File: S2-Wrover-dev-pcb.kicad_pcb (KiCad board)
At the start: 2 copper layers, 99.1 x 50 mm, 29 parts, among them J1 USB_C_Receptacle_USB2.0, J2 Jack-DC, P1 CONN_02X13, P3 CONN_02X13, SW1 RESET, SW2 BOOT, U1 MCP1700-1202E_SOT23, U2 ESP32-S2-WROVER, U3 TPS2113APW, U4 TP4056

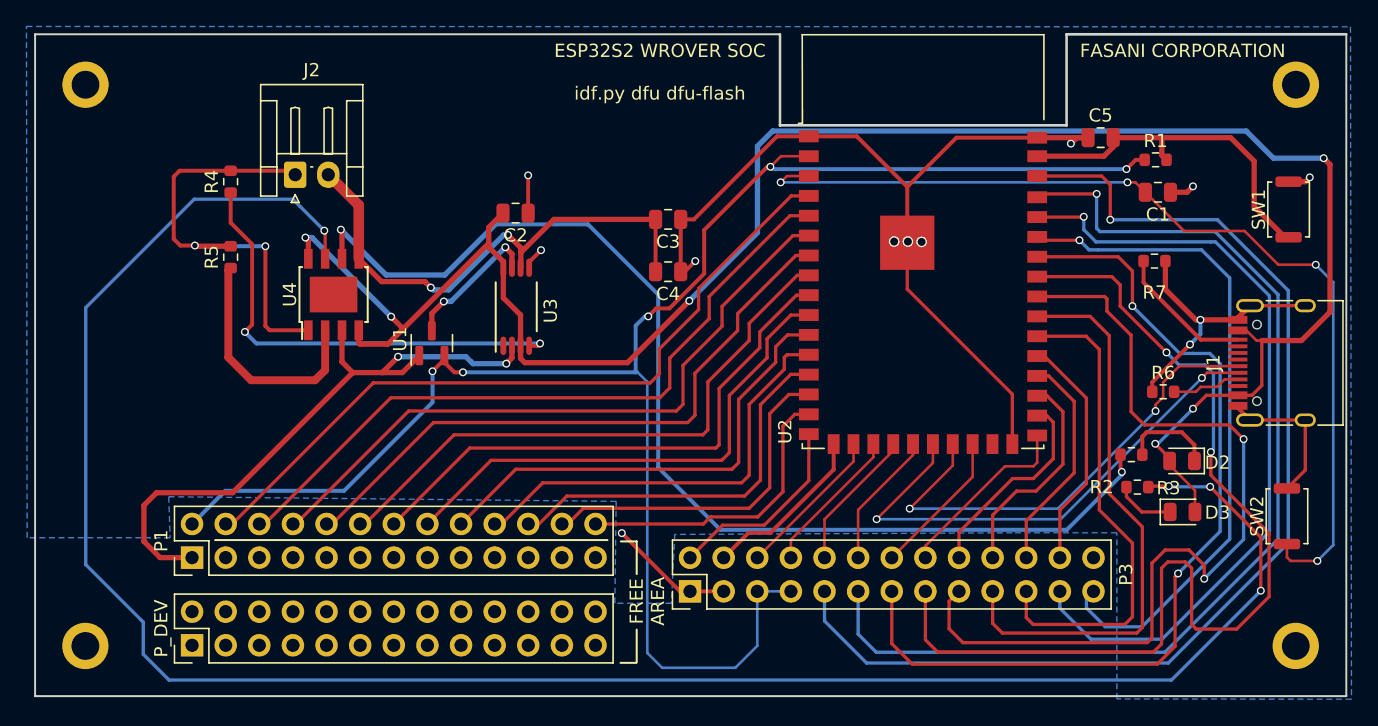
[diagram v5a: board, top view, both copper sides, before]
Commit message: Add IOs to silk
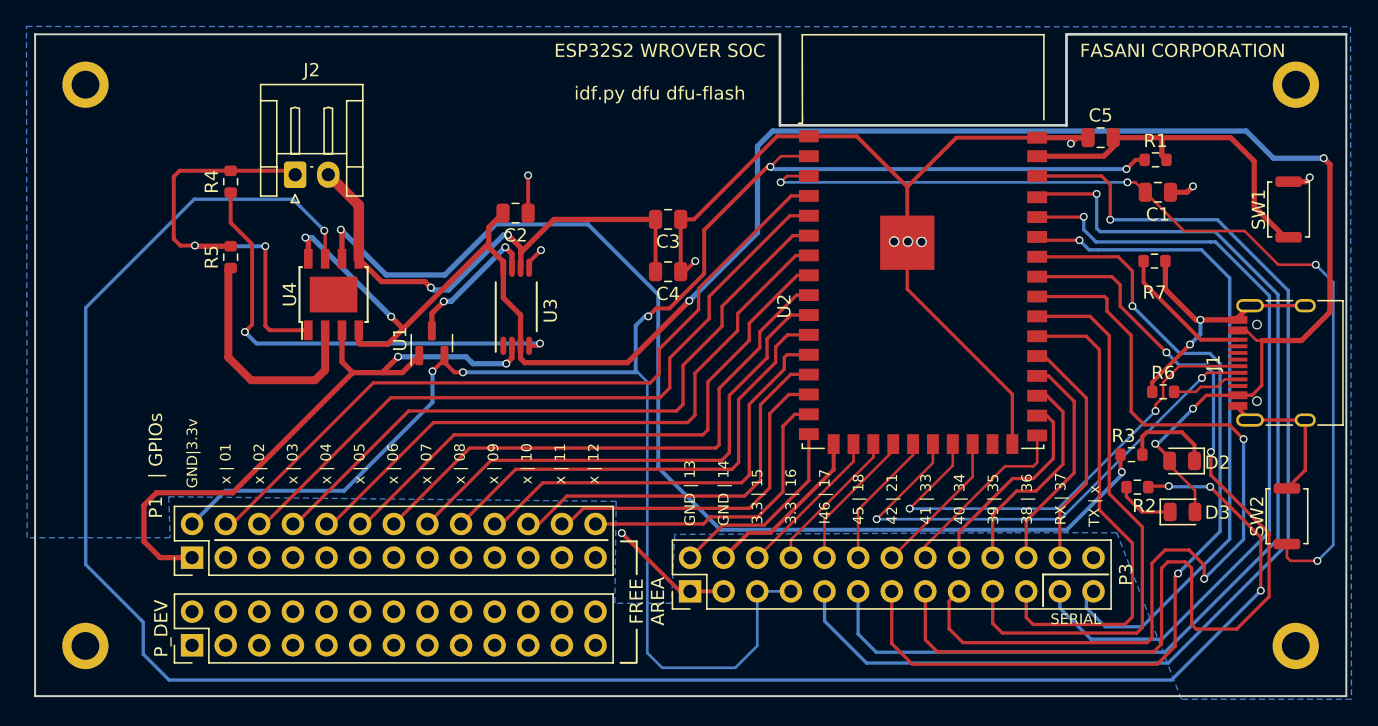
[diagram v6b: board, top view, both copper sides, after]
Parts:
- P1   | GPIOs: renamed from P1
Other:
- board text added: "3.3 | 15"
- board text added: "3.3 | 16"
- board text added: "38 | 36"
- board text added: "39 | 35"
- board text added: "40 | 34"
- board text added: "41 | 33"
- board text added: "42 | 21"
- board text added: "45 | 18"
- board text added: "GND | 13"
- board text added: "GND | 14"
- board text added: "GND|3.3v"
- board text added: "I46 | 17"
- board text added: "RX | 37"
- board text added: "SERIAL"
- board text added: "TX | x"
- board text added: "x | 01"
- board text added: "x | 02"
- board text added: "x | 03"
- board text added: "x | 04"
- board text added: "x | 05"
- board text added: "x | 06"
- board text added: "x | 07"
- board text added: "x | 08"
- board text added: "x | 09"
- board text added: "x | 10"
- board text added: "x | 11"
- board text added: "x | 12"
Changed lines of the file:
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@@
     (pad_to_mask_clearance 0)
     (aux_axis_origin 96.52 144.78)
-    (grid_origin 108.545 91.605)
+    (grid_origin 177.72 105.355)
     (pcbplotparams
       (layerselection 0x00000fc_80000001)
@@
     (property "Sheetname" "")
     (attr smd)
-    (fp_text reference "U2" (at -10.41 10.53 90) (layer "F.SilkS")
+    (fp_text reference "U2" (at -10.48 1.05 90) (layer "F.SilkS")
       (effects (font (size 1 1) (thickness 0.15)))
     )
@@
     (property "Sheetname" "")
     (attr smd)
-    (fp_text reference "R2" (at 2.25 -2.45) (layer "F.SilkS")
+    (fp_text reference "R2" (at -0.975 -3.875) (layer "F.SilkS")
       (effects (font (size 1 1) (thickness 0.15)))
     )
@@
       (effects (font (size 1 1) (thickness 0.15)))
     )
-    (fp_text value "MCP1700-1202E_SOT23" (at 0.465 2.175 90) (layer "F.Fab")
+    (fp_text value "MCP1700-1202E_SOT23" (at -2.8 5.775 180) (layer "F.Fab")
       (effects (font (size 1 1) (thickness 0.15)))
     )
@@
     (property "Sheetname" "")
     (attr through_hole)
-    (fp_text reference "P1" (at 1.27 -2.33 90) (layer "F.SilkS")
+    (fp_text reference "P1   | GPIOs" (at 6.95 -2.735 90) (layer "F.SilkS")
       (effects (font (size 1 1) (thickness 0.15)))
     )
@@
     (property "Sheetname" "")
     (attr smd)
-    (fp_text reference "R3" (at 2.35 0.075) (layer "F.SilkS")
+    (fp_text reference "R3" (at -1.05 -3.875) (layer "F.SilkS")
       (effects (font (size 1 1) (thickness 0.15)))
     )
@@
     )
   )
+  (gr_line (start 172.67 111.93) (end 172.67 114.33) (layer "F.SilkS") (width 0.15))
   (gr_line (start 110.12 109.33) (end 139.77 109.33) (layer "F.SilkS") (width 0.15))
   (gr_line (start 141.97 116.0925) (end 141.97 118.5675) (layer "F.SilkS") (width 0.15))
   (gr_line (start 141.97 109.43) (end 141.97 111.905) (layer "F.SilkS") (width 0.15))
   (gr_line (start 140.77 109.43) (end 141.97 109.43) (layer "F.SilkS") (width 0.15))
+  (gr_line (start 177.595 111.93) (end 172.67 111.93) (layer "F.SilkS") (width 0.15))
   (gr_line (start 140.745 118.605) (end 141.945 118.605) (layer "F.SilkS") (width 0.15))
   (gr_line (start 174.445 71.12) (end 195.58 71.12) (layer "Edge.Cuts") (width 0.2))
@@
   (gr_line (start 96.52 71.12) (end 96.52 121.12) (layer "Edge.Cuts") (width 0.15))
   (gr_line (start 174.445 78) (end 174.445 71.12) (layer "Edge.Cuts") (width 0.2))
+  (gr_text "x | 09" (at 131.138747 103.560953 90) (layer "F.SilkS")
+    (effects (font (size 0.8 0.8) (thickness 0.15)))
+  )
+  (gr_text "x | 10" (at 133.66583 103.560953 90) (layer "F.SilkS")
+    (effects (font (size 0.8 0.8) (thickness 0.15)))
+  )
+  (gr_text "RX | 37" (at 173.999163 106.218095 90) (layer "F.SilkS")
+    (effects (font (size 0.8 0.8) (thickness 0.15)))
+  )
+  (gr_text "x | 01" (at 110.922083 103.560953 90) (layer "F.SilkS")
+    (effects (font (size 0.8 0.8) (thickness 0.15)))
+  )
+  (gr_text "42 | 21" (at 161.269998 106.237143 90) (layer "F.SilkS")
+    (effects (font (size 0.8 0.8) (thickness 0.15)))
+  )
+  (gr_text "3.3 | 16" (at 153.632499 106.046666 90) (layer "F.SilkS")
+    (effects (font (size 0.8 0.8) (thickness 0.15)))
+  )
+  (gr_text "x | 07" (at 126.084581 103.560953 90) (layer "F.SilkS")
+    (effects (font (size 0.8 0.8) (thickness 0.15)))
+  )
+  (gr_text "SERIAL" (at 175.145 115.305) (layer "F.SilkS")
+    (effects (font (size 0.8 0.8) (thickness 0.1)))
+  )
+  (gr_text "x | 03" (at 115.976249 103.560953 90) (layer "F.SilkS")
+    (effects (font (size 0.8 0.8) (thickness 0.15)))
+  )
+  (gr_text "x | 02" (at 113.449166 103.560953 90) (layer "F.SilkS")
+    (effects (font (size 0.8 0.8) (thickness 0.15)))
+  )
+  (gr_text "GND | 13" (at 145.995 105.78 90) (layer "F.SilkS")
+    (effects (font (size 0.8 0.8) (thickness 0.15)))
+  )
+  (gr_text "GND | 14" (at 148.540833 105.78 90) (layer "F.SilkS")
+    (effects (font (size 0.8 0.8) (thickness 0.15)))
+  )
+  (gr_text "3.3 | 15" (at 151.086666 106.046666 90) (layer "F.SilkS")
+    (effects (font (size 0.8 0.8) (thickness 0.15)))
+  )
+  (gr_text "x | 08" (at 128.611664 103.560953 90) (layer "F.SilkS")
+    (effects (font (size 0.8 0.8) (thickness 0.15)))
+  )
+  (gr_text "38 | 36" (at 171.45333 106.237143 90) (layer "F.SilkS")
+    (effects (font (size 0.8 0.8) (thickness 0.15)))
+  )
+  (gr_text "39 | 35" (at 168.907497 106.237143 90) (layer "F.SilkS")
+    (effects (font (size 0.8 0.8) (thickness 0.15)))
+  )
+  (gr_text "x | 12" (at 138.72 103.560953 90) (layer "F.SilkS")
+    (effects (font (size 0.8 0.8) (thickness 0.15)))
+  )
   (gr_text "ESP32S2 WROVER SOC\n\nidf.py dfu dfu-flash" (at 143.72 73.98) (layer "F.SilkS")
     (effects (font (size 1 1) (thickness 0.15)))
   )
+  (gr_text "TX | x" (at 176.545 106.751428 90) (layer "F.SilkS")
+    (effects (font (size 0.8 0.8) (thickness 0.15)))
+  )
   (gr_text "FASANI CORPORATION" (at 183.22 72.37) (layer "F.SilkS")
     (effects (font (size 1 1) (thickness 0.15)))
   )
+  (gr_text "x | 05" (at 121.030415 103.560953 90) (layer "F.SilkS")
+    (effects (font (size 0.8 0.8) (thickness 0.15)))
+  )
+  (gr_text "45 | 18" (at 158.724165 106.237143 90) (layer "F.SilkS")
+    (effects (font (size 0.8 0.8) (thickness 0.15)))
+  )
   (gr_text "FREE\nAREA" (at 142.77 113.955 90) (layer "F.SilkS")
     (effects (font (size 1 1) (thickness 0.15)))
+  )
+  (gr_text "x | 04" (at 118.503332 103.560953 90) (layer "F.SilkS")
+    (effects (font (size 0.8 0.8) (thickness 0.15)))
+  )
+  (gr_text "40 | 34" (at 166.361664 106.237143 90) (layer "F.SilkS")
+    (effects (font (size 0.8 0.8) (thickness 0.15)))
+  )
+  (gr_text "x | 06" (at 123.557498 103.560953 90) (layer "F.SilkS")
+    (effects (font (size 0.8 0.8) (thickness 0.15)))
+  )
+  (gr_text "GND|3.3v" (at 108.395 102.78 90) (layer "F.SilkS")
+    (effects (font (size 0.8 0.8) (thickness 0.15)))
+  )
+  (gr_text "41 | 33" (at 163.815831 106.237143 90) (layer "F.SilkS")
+    (effects (font (size 0.8 0.8) (thickness 0.15)))
+  )
+  (gr_text "x | 11" (at 136.192913 103.560953 90) (layer "F.SilkS")
+    (effects (font (size 0.8 0.8) (thickness 0.15)))
+  )
+  (gr_text "I46 | 17" (at 156.178332 106.046666 90) (layer "F.SilkS")
+    (effects (font (size 0.8 0.8) (thickness 0.15)))
   )
   (target plus (at 96.51 121.14) (size 5) (width 0.15) (layer "Edge.Cuts"))
@@
       (pts
         (xy 195.97 121.355)
-        (xy 178.245 121.33)
+        (xy 183.12 121.355)
         (xy 178.245 108.78)
         (xy 170.3575 108.78)

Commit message: v1.1 clean
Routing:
- net Net-(J1-PadA7): track 39.3 -> 42.7 mm
- net Net-(J1-PadA6): track 36.4 -> 39.1 mm
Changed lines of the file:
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@@
   (segment (start 129.07 95.48) (end 123.945 95.48) (width 0.4) (layer "B.Cu") (net 1))
   (segment (start 108.645 87.13) (end 108.595 87.08) (width 0.3) (layer "B.Cu") (net 1))
+  (segment (start 182.9575 96.1925) (end 185.5825 96.1925) (width 0.2) (layer "F.Cu") (net 2))
   (segment (start 181.745 97.405) (end 182.9575 96.1925) (width 0.2) (layer "F.Cu") (net 2))
   (segment (start 165.85 102.08) (end 165.85 103.7) (width 0.2) (layer "F.Cu") (net 2))
-  (segment (start 182.9575 96.1925) (end 187.385 96.1925) (width 0.2) (layer "F.Cu") (net 2))
+  (segment (start 185.8075 95.1925) (end 185.5825 95.4175) (width 0.2) (layer "F.Cu") (net 2))
+  (segment (start 187.385 95.1925) (end 185.8075 95.1925) (width 0.2) (layer "F.Cu") (net 2))
+  (segment (start 185.5825 95.4175) (end 185.5825 96.1925) (width 0.2) (layer "F.Cu") (net 2))
   (segment (start 181.17 99.105) (end 181.745 98.53) (width 0.2) (layer "F.Cu") (net 2))
+  (segment (start 185.5825 96.1925) (end 187.385 96.1925) (width 0.2) (layer "F.Cu") (net 2))
   (segment (start 181.17 99.58) (end 181.17 99.105) (width 0.2) (layer "F.Cu") (net 2))
   (segment (start 165.85 103.7) (end 162.595 106.955) (width 0.2) (layer "F.Cu") (net 2))
@@
   (segment (start 184.5825 94.1925) (end 180.2625 89.8725) (width 0.3) (layer "F.Cu") (net 3))
   (segment (start 180.2625 89.8725) (end 180.2625 88.255) (width 0.3) (layer "F.Cu") (net 3))
+  (segment (start 188.72 95.905) (end 188.72 96.48) (width 0.2) (layer "F.Cu") (net 5))
+  (segment (start 188.72 96.48) (end 188.5075 96.6925) (width 0.2) (layer "F.Cu") (net 5))
+  (segment (start 187.385 95.6925) (end 188.5075 95.6925) (width 0.2) (layer "F.Cu") (net 5))
+  (segment (start 188.5075 96.6925) (end 187.385 96.6925) (width 0.2) (layer "F.Cu") (net 5))
   (segment (start 164.35 102.08) (end 164.35 103.5) (width 0.2) (layer "F.Cu") (net 5))
   (segment (start 185.0575 96.6925) (end 184.67 97.08) (width 0.2) (layer "F.Cu") (net 5))
   (segment (start 164.35 103.5) (end 160.095 107.755) (width 0.2) (layer "F.Cu") (net 5))
   (segment (start 187.385 96.6925) (end 185.0575 96.6925) (width 0.2) (layer "F.Cu") (net 5))
+  (segment (start 188.5075 95.6925) (end 188.72 95.905) (width 0.2) (layer "F.Cu") (net 5))
   (via (at 184.67 97.08) (size 0.6) (drill 0.4) (layers "F.Cu" "B.Cu") (net 5))
   (via (at 160.095 107.755) (size 0.6) (drill 0.4) (layers "F.Cu" "B.Cu") (net 5))
@@
   (segment (start 133.195001 94.655002) (end 133.195001 95.605001) (width 0.4) (layer "F.Cu") (net 8))
   (segment (start 123.17 94.53) (end 124.3575 93.3425) (width 0.4) (layer "F.Cu") (net 8))
-  (segment (start 189.195 97.655) (end 189.195 94.255) (width 0.25) (layer "F.Cu") (net 8))
   (segment (start 184.145 105.58) (end 184.145 107.205) (width 0.2) (layer "F.Cu") (net 8))
   (segment (start 120.975 94.435) (end 121.07 94.53) (width 0.4) (layer "F.Cu") (net 8))
   (segment (start 188.795 94.255) (end 189.195 94.255) (width 0.2) (layer "F.Cu") (net 8))
-  (segment (start 188.4575 98.3925) (end 189.195 97.655) (width 0.25) (layer "F.Cu") (net 8))
+  (segment (start 190.095 94.255) (end 189.195 94.255) (width 0.4) (layer "F.Cu") (net 8))
+  (segment (start 190.245 94.255) (end 190.095 94.255) (width 0.4) (layer "F.Cu") (net 8))
   (segment (start 187.385 93.4925) (end 188.0325 93.4925) (width 0.2) (layer "F.Cu") (net 8))
   (segment (start 121.07 94.53) (end 123.17 94.53) (width 0.4) (layer "F.Cu") (net 8))
@@
   (segment (start 131.895001 88.755001) (end 131.895001 91.030001) (width 0.4) (layer "F.Cu") (net 8))
   (segment (start 130.795 86.905) (end 130.795 85.705) (width 0.4) (layer "F.Cu") (net 8))
+  (segment (start 188.1325 98.3925) (end 190.095 96.43) (width 0.25) (layer "F.Cu") (net 8))
   (segment (start 194.345 92.105) (end 192.195 94.255) (width 0.4) (layer "F.Cu") (net 8))
+  (segment (start 187.385 98.3925) (end 188.1325 98.3925) (width 0.25) (layer "F.Cu") (net 8))
   (segment (start 124.3575 93.3425) (end 130.795 86.905) (width 0.4) (layer "F.Cu") (net 8))
+  (segment (start 190.095 96.43) (end 190.095 94.255) (width 0.25) (layer "F.Cu") (net 8))
   (segment (start 181.145 102.055) (end 182.23 103.14) (width 0.25) (layer "F.Cu") (net 8))
   (segment (start 130.795 87.205) (end 130.795 86.905) (width 0.4) (layer "F.Cu") (net 8))
   (segment (start 130.795 85.705) (end 131.87 84.63) (width 0.4) (layer "F.Cu") (net 8))
   (segment (start 182.23 103.665) (end 184.145 105.58) (width 0.2) (layer "F.Cu") (net 8))
-  (segment (start 192.195 94.255) (end 189.195 94.255) (width 0.4) (layer "F.Cu") (net 8))
   (segment (start 194.345 92.105) (end 194.345 80.955) (width 0.4) (layer "F.Cu") (net 8))
   (segment (start 133.195001 92.330001) (end 133.195001 94.655002) (width 0.4) (layer "F.Cu") (net 8))
-  (segment (start 187.385 98.3925) (end 188.4575 98.3925) (width 0.25) (layer "F.Cu") (net 8))
   (segment (start 131.895001 91.030001) (end 133.195001 92.330001) (width 0.4) (layer "F.Cu") (net 8))
   (segment (start 133.195001 95.605001) (end 133.52 95.93) (width 0.4) (layer "F.Cu") (net 8))
+  (segment (start 192.195 94.255) (end 190.245 94.255) (width 0.4) (layer "F.Cu") (net 8))
   (segment (start 124.3075 93.3425) (end 124.3575 93.3425) (width 0.4) (layer "F.Cu") (net 8))
   (segment (start 131.895001 88.305001) (end 130.795 87.205) (width 0.4) (layer "F.Cu") (net 8))
